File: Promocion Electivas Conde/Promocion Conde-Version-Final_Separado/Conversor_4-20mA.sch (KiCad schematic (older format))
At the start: 11 parts

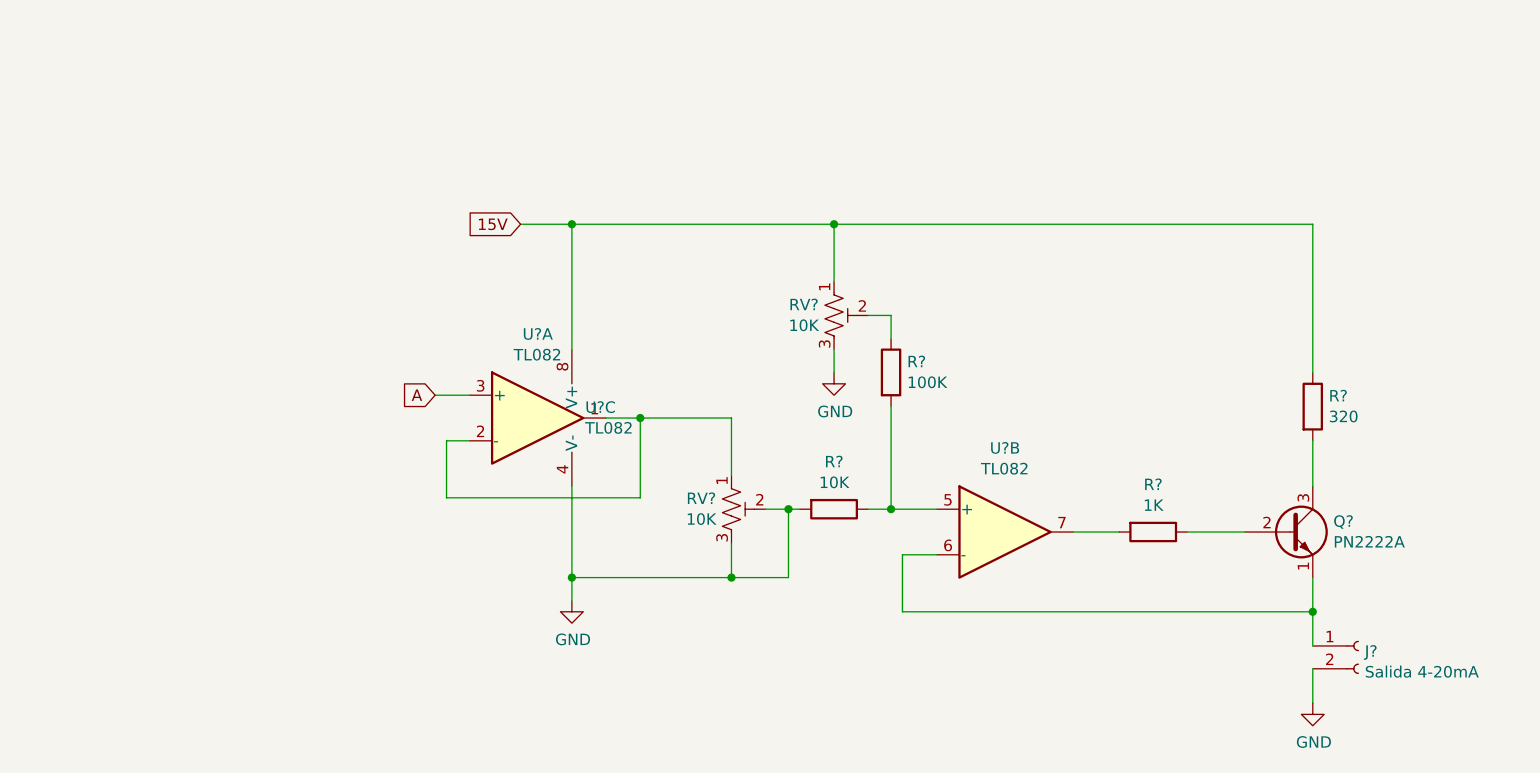
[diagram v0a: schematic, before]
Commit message: Agregue circuito 4-20 mA a la version en bloques
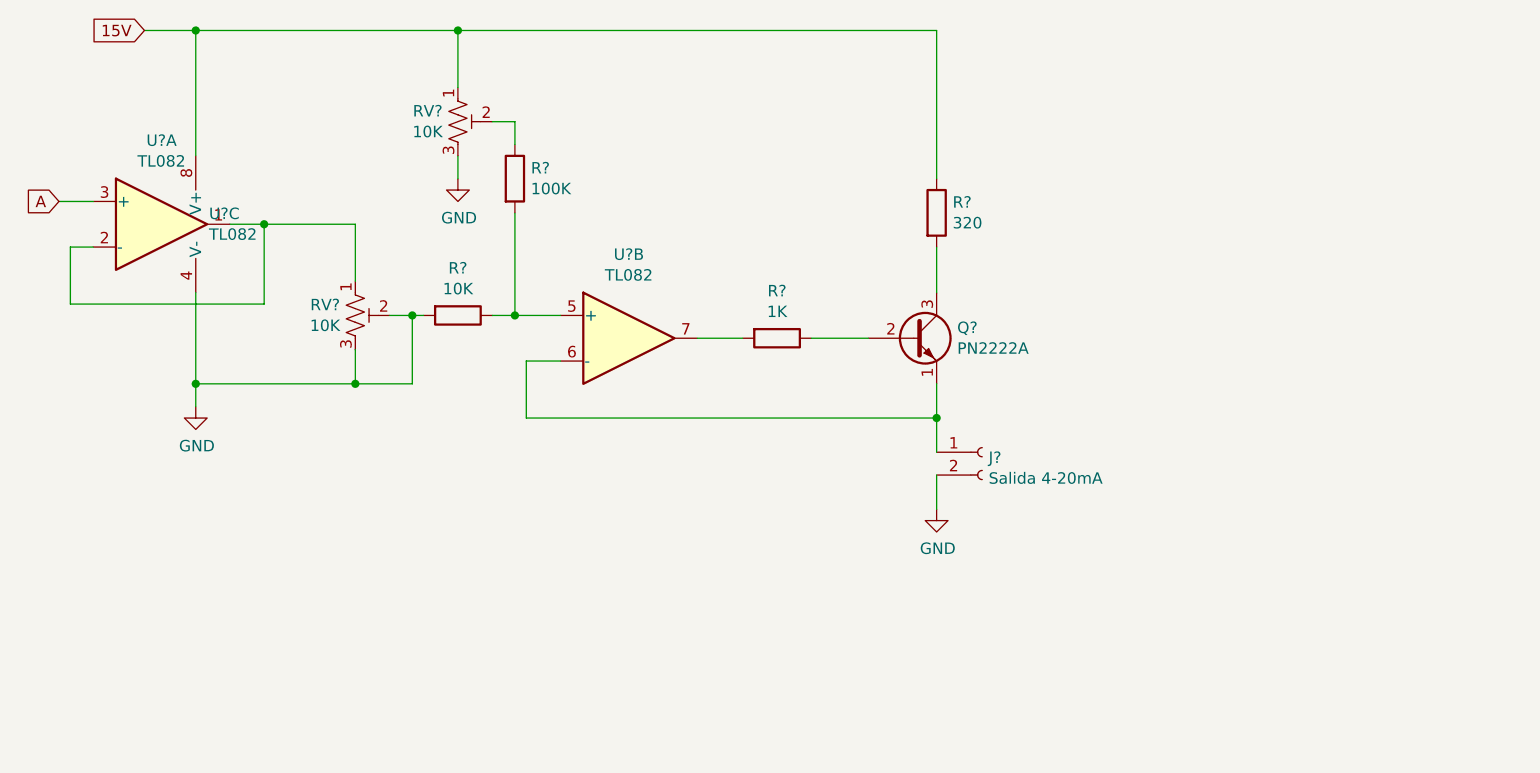
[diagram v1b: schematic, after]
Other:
- moved on the sheet: J?, Q?, R?, RV?, U?A, U?B, U?C
